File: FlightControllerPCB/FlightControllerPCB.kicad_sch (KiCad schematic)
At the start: 0 parts

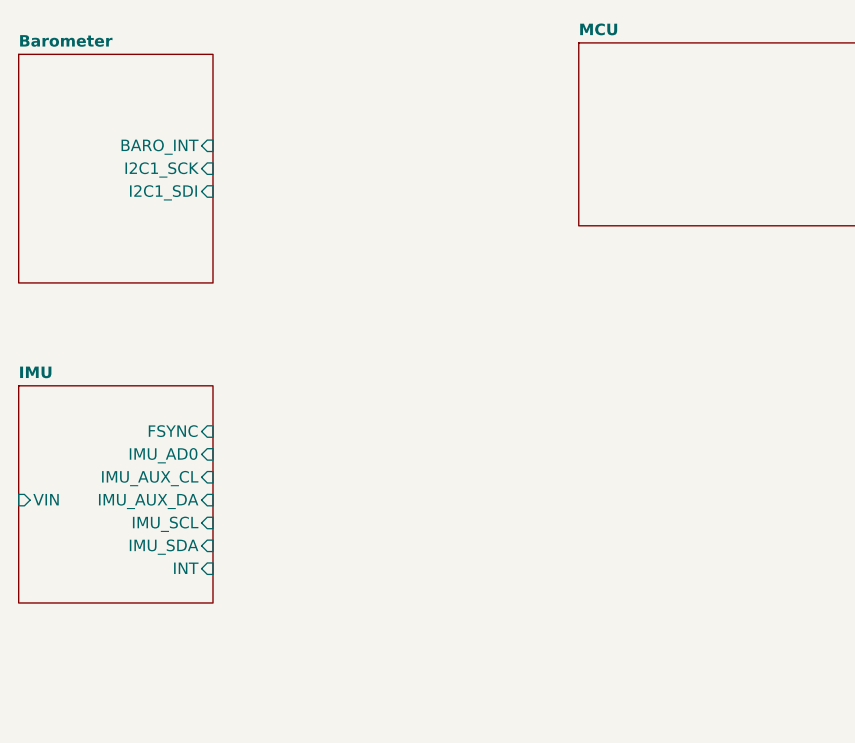
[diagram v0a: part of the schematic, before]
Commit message: initial baro/imu to mcu pins
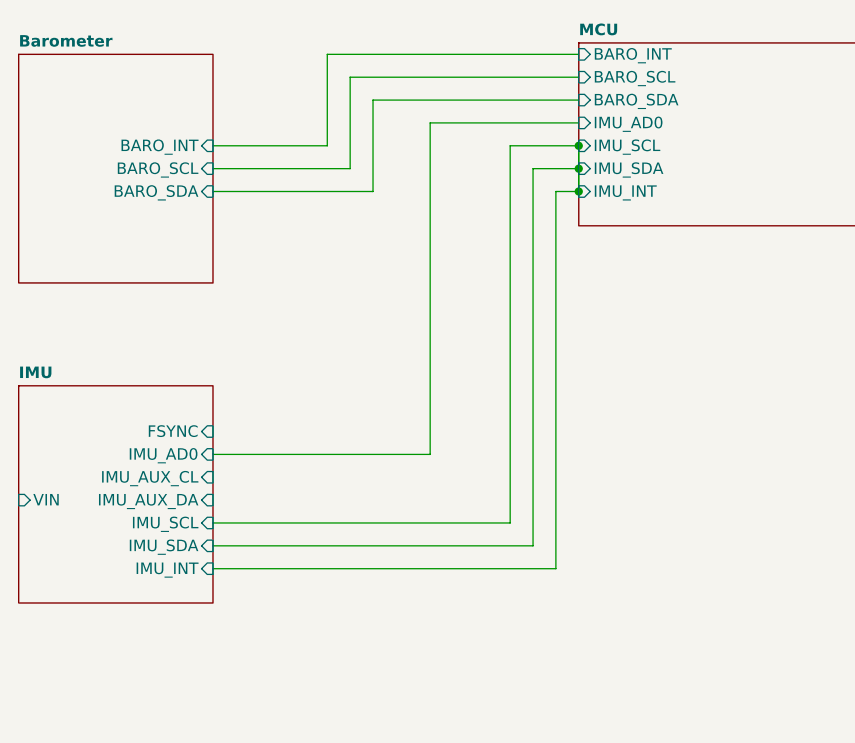
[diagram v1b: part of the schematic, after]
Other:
- sheet Barometer ports: added BARO_SCL, BARO_SDA; removed I2C1_SCK, I2C1_SDI
- sheet IMU ports: added IMU_INT; removed INT
- sheet MCU ports: added BARO_INT, BARO_SCL, BARO_SDA, IMU_AD0, IMU_INT, IMU_SCL, IMU_SDA; removed none

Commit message: actually the IMU+baro changes
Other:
- sheet IMU ports: added none; removed IMU_AUX_CL, IMU_AUX_DA, VIN
- sheet MCU ports: added FSYNC; removed none

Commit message: Power circuit
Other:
- sheet MCU ports: added IMU_FSYNC; removed FSYNC
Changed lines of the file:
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@@
 			)
 		)
-		(pin "FSYNC" input
+		(pin "IMU_FSYNC" input
 			(at 81.28 25.4 180)
 			(effects

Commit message: early MCU setup
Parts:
- added J2: Jetson Conn, symbol Connector:Conn_01x04_Socket
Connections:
- new net MCU/SBC CTS: J2.4 (Pin_4)
- new net MCU/SBC RTS: J2.3 (Pin_3)
- new net MCU/SBC RX: J2.2 (Pin_2)
- new net MCU/SBC TX: J2.1 (Pin_1)
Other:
- sheet MCU ports: added SBC CTS, SBC RTS, SBC RX, SBC TX, SWDCLK, SWDIO, USB Data +, USB Data -; removed none
- sheet USB+POWER ports: added USB Data +, USB Data -; removed none

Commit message: Sanity check+Error fixes
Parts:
- added J1: GPS+mag conn, symbol Connector:Conn_01x06_Socket
- added J3: RC conn, symbol Connector:Conn_01x04_Socket
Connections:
- new net +5V: J1.2 (Pin_2), J3.2 (Pin_2)
- new net GND: J1.1 (Pin_1), J3.1 (Pin_1)
- new net MCU/GPS_RX: J1.4 (Pin_4)
- new net MCU/GPS_SCL: J1.6 (Pin_6)
- new net MCU/GPS_SDA: J1.5 (Pin_5)
- new net MCU/GPS_TX: J1.3 (Pin_3)
- new net MCU/RC_RX: J3.4 (Pin_4)
- new net MCU/RC_TX: J3.3 (Pin_3)
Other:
- sheet MCU ports: added GPS_RX, GPS_SCL, GPS_SDA, GPS_TX, RC_RX, RC_TX; removed none
